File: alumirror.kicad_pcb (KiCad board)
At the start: 2 copper layers, 139.7 x 87.2 mm, 90 parts, among them J1 USB_C_Receptacle_USB2.0_16P_2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, J2 USB_C_Receptacle_USB2.0_16P_2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, J3 USB_C_Receptacle_USB2.0_16P_2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, J4 USB_C_Receptacle_USB2.0_16P_2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, K00 PG1350, K01 PG1350, K02 PG1350, K03 PG1350, K04 PG1350, K05 PG1350, K10 PG1350, K11 PG1350, K12 PG1350, K13 PG1350, K14 PG1350, K15 PG1350, K20 PG1350, K21 PG1350, K22 PG1350, K23 PG1350, K24 PG1350, K25 PG1350_1½U, K30 PG1350_1½U, K31 PG1350/SKQUCAA010, SW1 BOOT, U1 CH552T, U2 CH552T, U3 USBLC6-2P6, U4 USBLC6-2P6, U5 USBLC6-2P6, U6 USBLC6-2P6

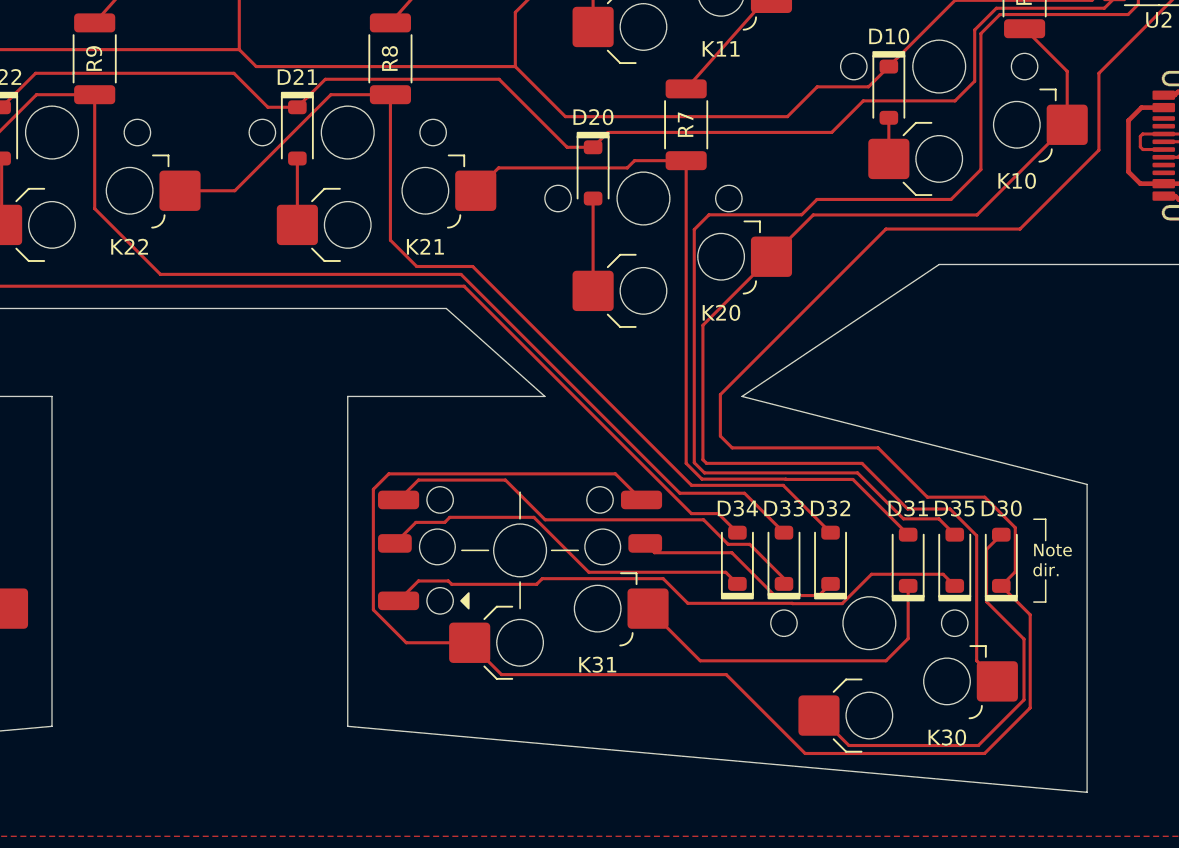
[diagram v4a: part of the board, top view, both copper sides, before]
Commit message: Rotate D31–35 90º
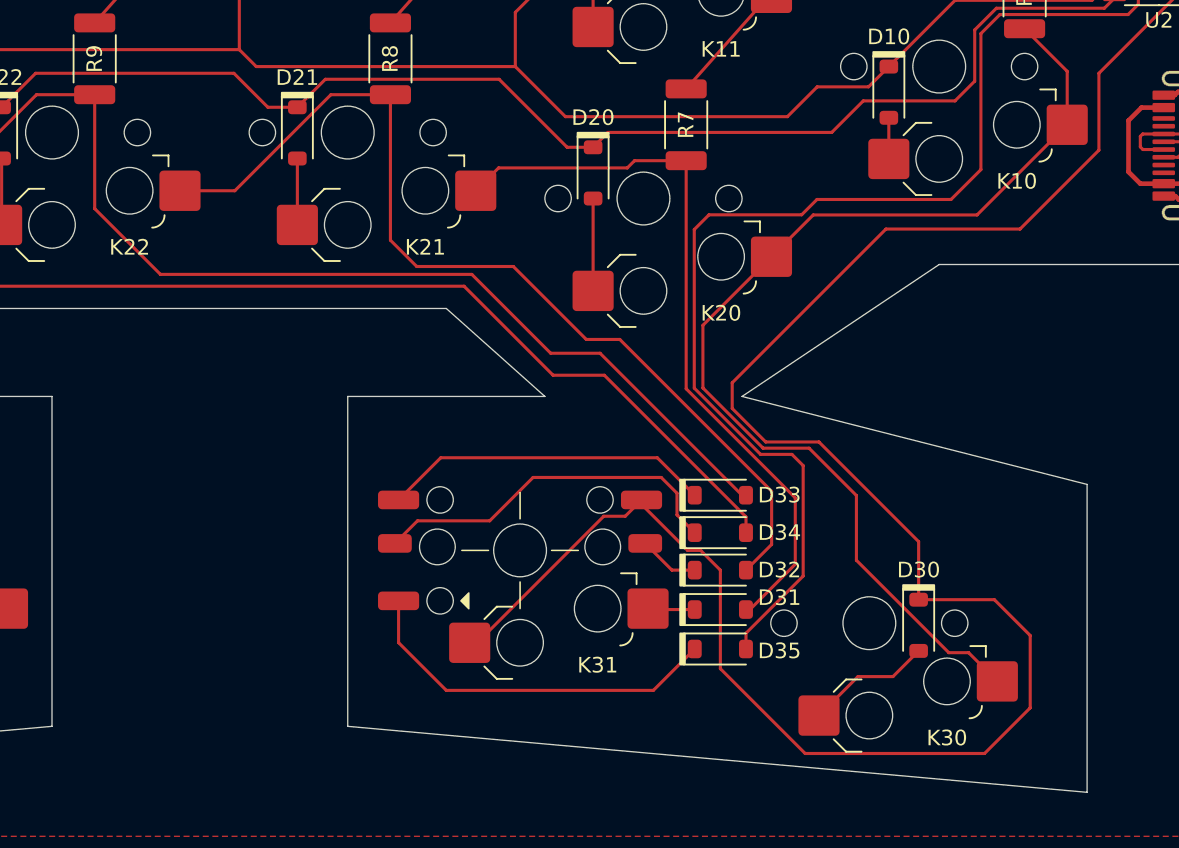
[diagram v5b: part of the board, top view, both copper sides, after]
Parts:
- moved D35 16.1 mm to (185.9, 106.9), turned to 0 degrees
- moved D31 12.5 mm to (185.9, 104.4), turned to 0 degrees
- moved D32 7.14 mm to (185.9, 101.9), turned to 0 degrees
- moved D30 6.77 mm to (198.7, 105.4), turned to -90 degrees
- moved D33 5.77 mm to (185.9, 97.0), turned to 0 degrees
- moved D34 1.98 mm to (185.9, 99.4), turned to 0 degrees
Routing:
- net Row3R: track 155.0 -> 129.1 mm
- net Net-(D30-A): track 27.3 -> 8.14 mm
- net Net-(D31-K): track 22.1 -> 3.03 mm
- net Net-(D35-K): track 38.4 -> 24.1 mm
- net Net-(D32-K): track 13.6 -> 3.90 mm
- net Net-(D33-K): track 28.0 -> 21.2 mm
- net Col0T: track 74.4 -> 69.4 mm
- net Col3RT: track 78.0 -> 74.6 mm
- net Col1RT: track 50.1 -> 47.6 mm
- net Net-(D34-K): track 24.5 -> 23.4 mm
- net Col4T: track 102.7 -> 103.9 mm
- net Col5: track 227.6 -> 226.5 mm
- net Col2RT: track 61.6 -> 62.5 mm
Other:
- board text removed: "Note dir."

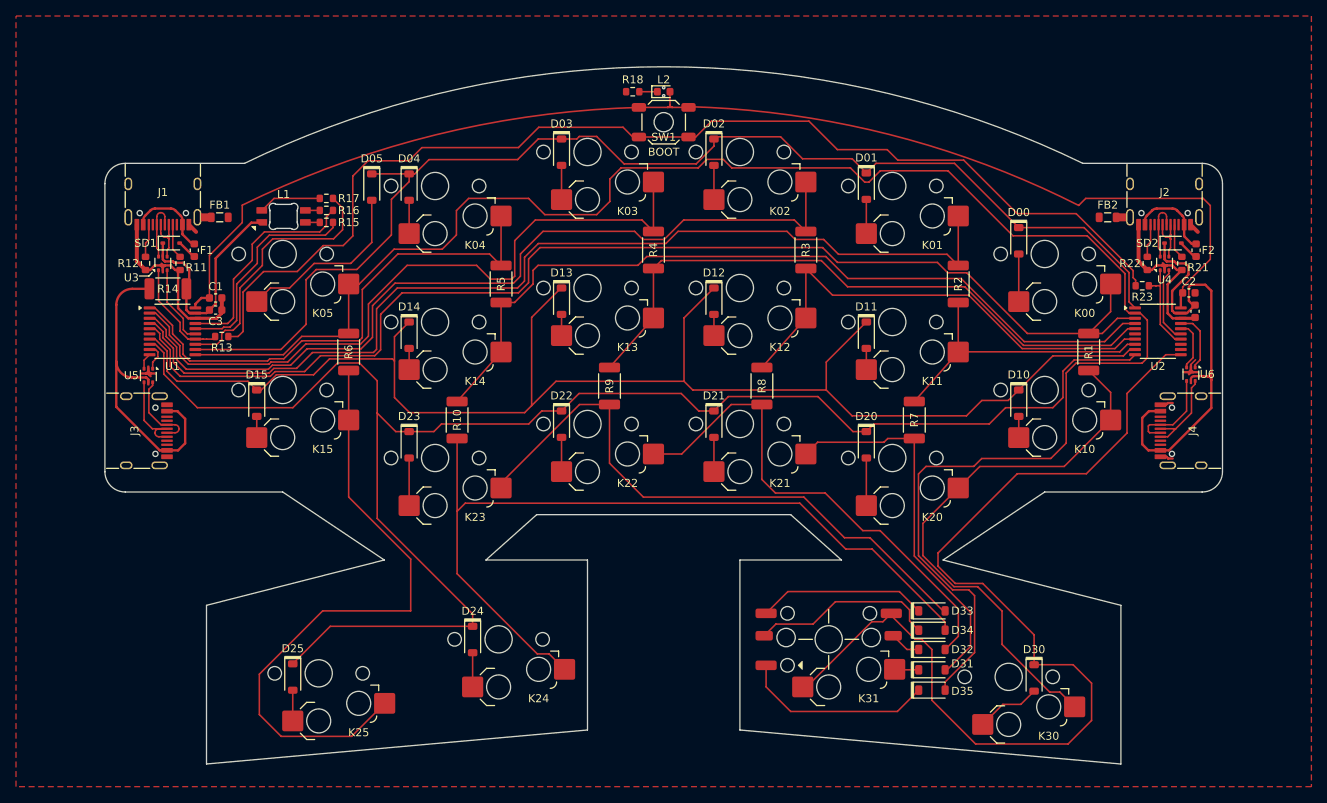
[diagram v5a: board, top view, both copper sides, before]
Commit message: Convert 3D model cutout outlines to polygons
This gives more flexibility to the shapes and is less clutter on the board.
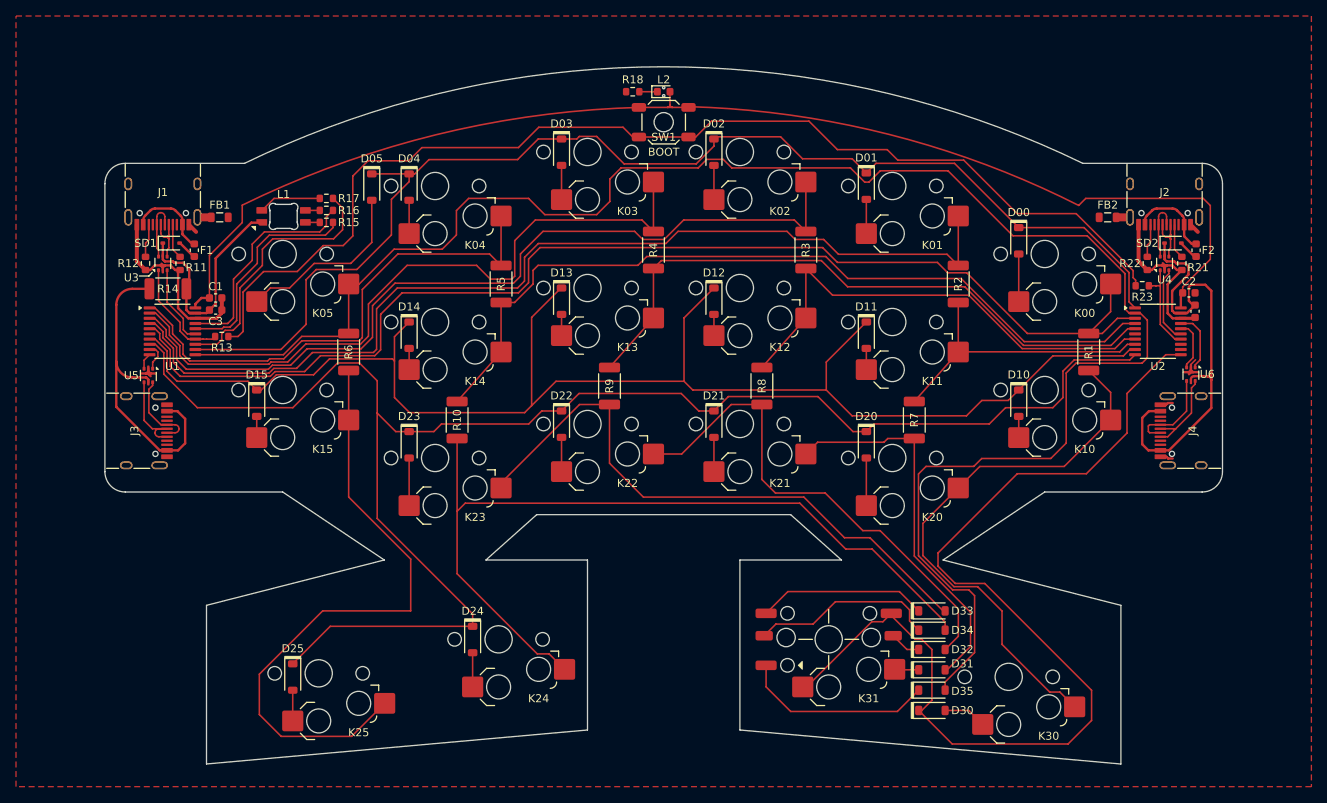
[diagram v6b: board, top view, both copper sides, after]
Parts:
- moved D30 13.4 mm to (185.9, 109.5), turned to 0 degrees
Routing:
- net Net-(D30-A): track 8.14 -> 5.43 mm
- net Row3R: track 129.1 -> 129.6 mm

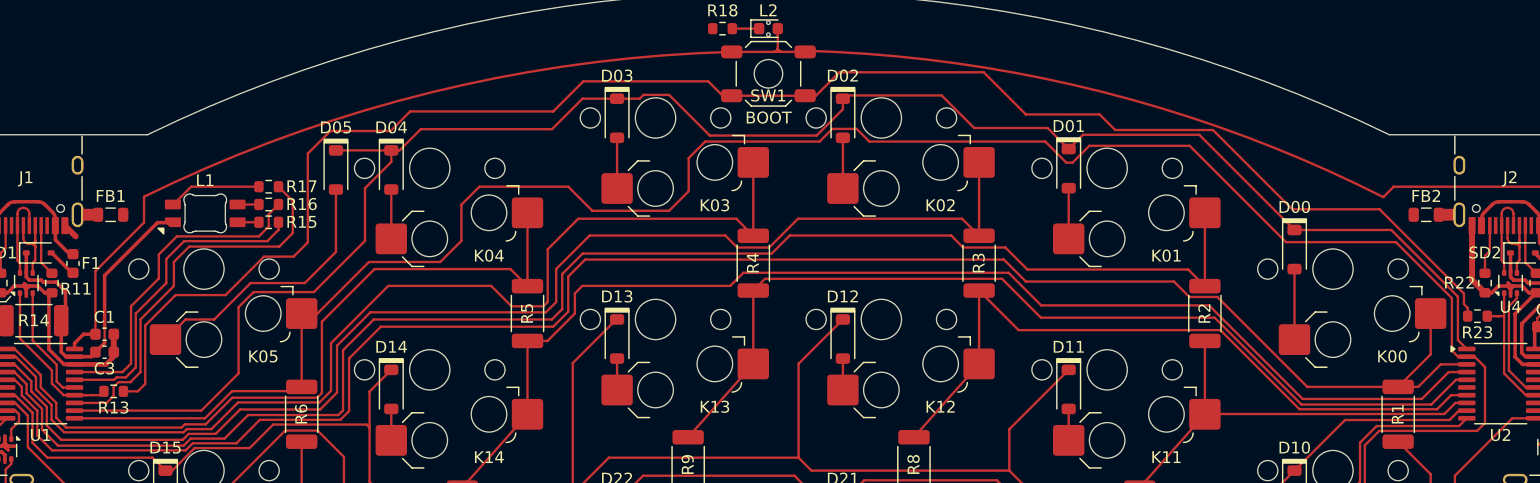
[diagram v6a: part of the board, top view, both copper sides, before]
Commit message: Replace three-colour RGB LED with SK6812MINI-E
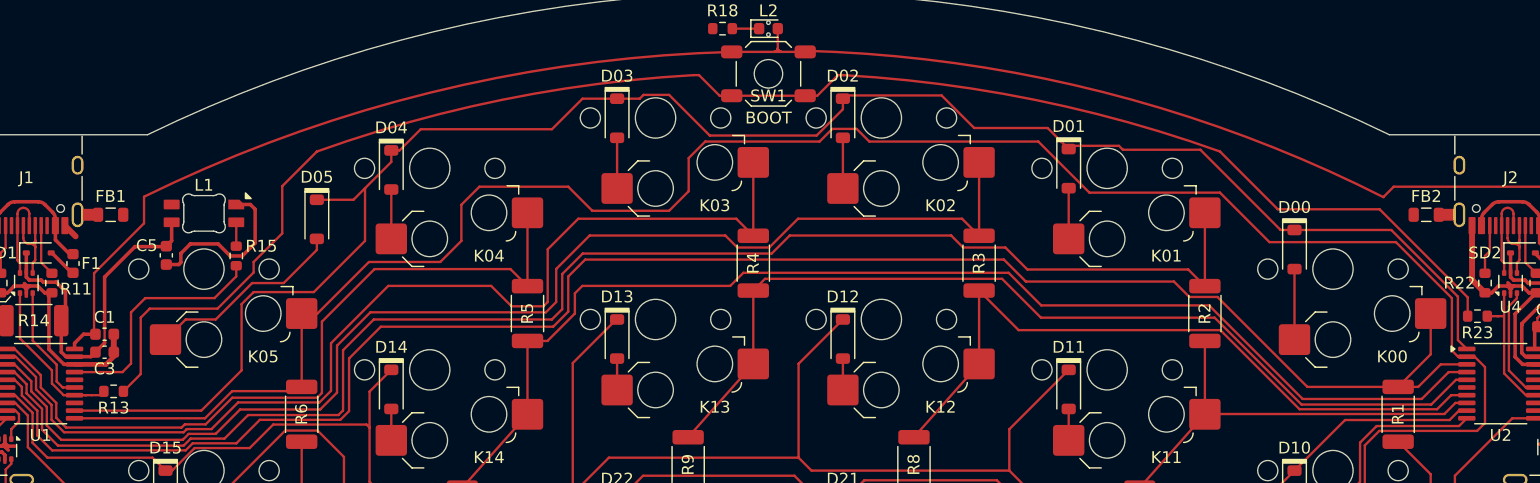
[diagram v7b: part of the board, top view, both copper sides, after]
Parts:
- removed R16, R17: R, Project Library:R_0603_1608Metric_Mod
- added C5: 100µF, Capacitor_SMD:C_0603_1608Metric, F.Cu at (101.6, 51.3)
- R15: value R -> 470
- moved D05 4.46 mm to (114.3, 48.2)
- moved R15 3.94 mm to (107.5, 51.3), turned to 90 degrees
- moved L1 0.11 mm to (104.8, 47.7), turned to 180 degrees
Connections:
- L1 pad 1: Net-(L1-GK) -> VCC_L
- L1 pad 2: Net-(L1-RK) -> unconnected-(L1-DOUT-Pad2)
- L1 pad 3: Net-(L1-BK) -> Net-(L1-DIN)
- L1 pad 4: VCC_L -> GND
- R15 pad 1: LED_R -> LED
- R15 pad 2: Net-(L1-RK) -> Net-(L1-DIN)
- U1 pad 13: LED_B -> unconnected-(U1-P3.5-Pad13)
- U1 pad 16: LED_R -> unconnected-(U1-P1.3-Pad16)
- U1 pad 17: LED_G -> LED
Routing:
- net BOOT: track 141.5 -> 72.0 mm
- net LED_B: track 33.2 -> 0.00 mm
- net LED_G: track 27.9 -> 0.00 mm
- net LED_R: track 27.1 -> 0.00 mm
- net LED: track 0.00 -> 20.6 mm
- net GND: track 60.9 -> 75.1 mm
- net Net-(L1-BK): track 7.84 -> 0.00 mm
- net Net-(D05-A): track 22.7 -> 16.8 mm
- net Net-(L1-DIN): track 0.00 -> 2.02 mm
- net Net-(L1-RK): track 1.80 -> 0.00 mm
- net Net-(L1-GK): track 1.80 -> 0.00 mm
- net Col5: track 226.5 -> 225.3 mm
- net Row0: track 154.6 -> 153.6 mm
- net VCC_L: track 28.0 -> 28.7 mm

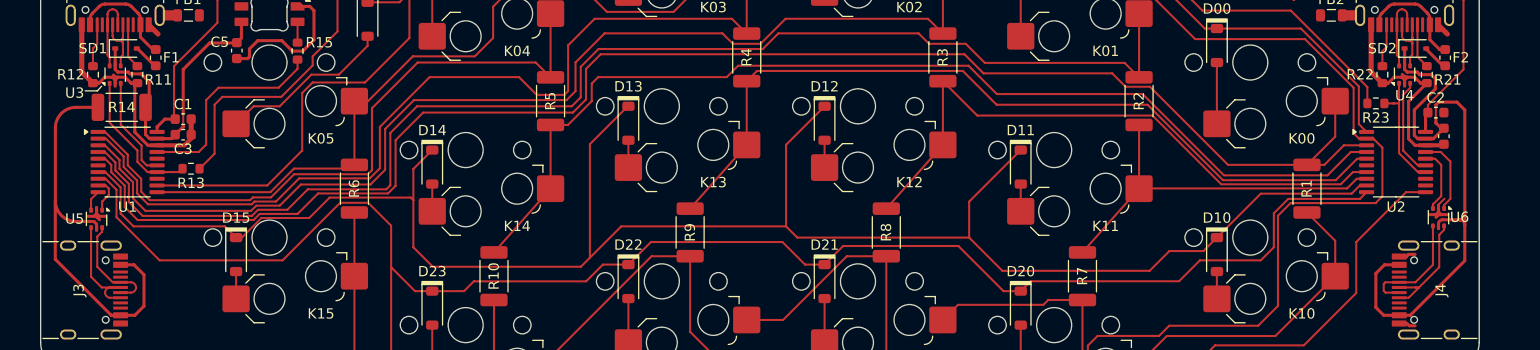
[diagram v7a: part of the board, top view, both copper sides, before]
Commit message: Add custom SOT-666 footprint
Footprint has ground routing and 3D cutout
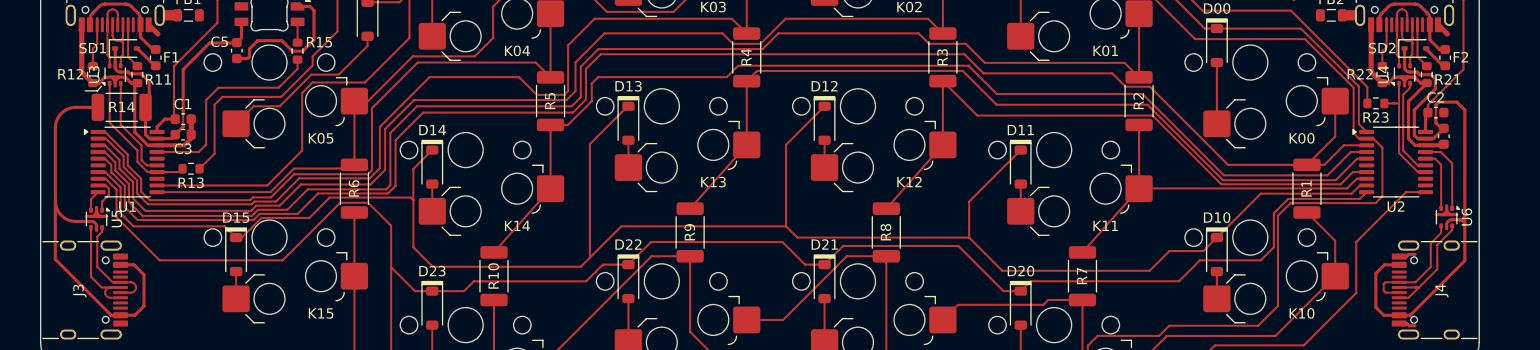
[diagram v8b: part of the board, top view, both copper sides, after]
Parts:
- U3, U4, U5, U6: footprint Package_TO_SOT_SMD:SOT-666 -> Project Library:SOT-666_Mod
- moved U6 0.79 mm to (219.1, 67.4)
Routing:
- net GND: track 75.1 -> 65.2 mm
- net VCC_R: track 56.4 -> 55.7 mm
